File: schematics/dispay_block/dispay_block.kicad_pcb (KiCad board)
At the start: 2 copper layers, 100 x 53.5 mm, 292 parts, among them J1 Conn_02x10_Odd_Even, J2 Conn_02x10_Odd_Even, J3 Conn_02x01, Q1 BC847BS, Q2 BC847BS, Q3 BC847BS, Q4 BC847BS, Q5 BC847BS, Q6 BC847BS, Q7 BC847BS, Q8 BC847BS, U1 CH32V003FxUx

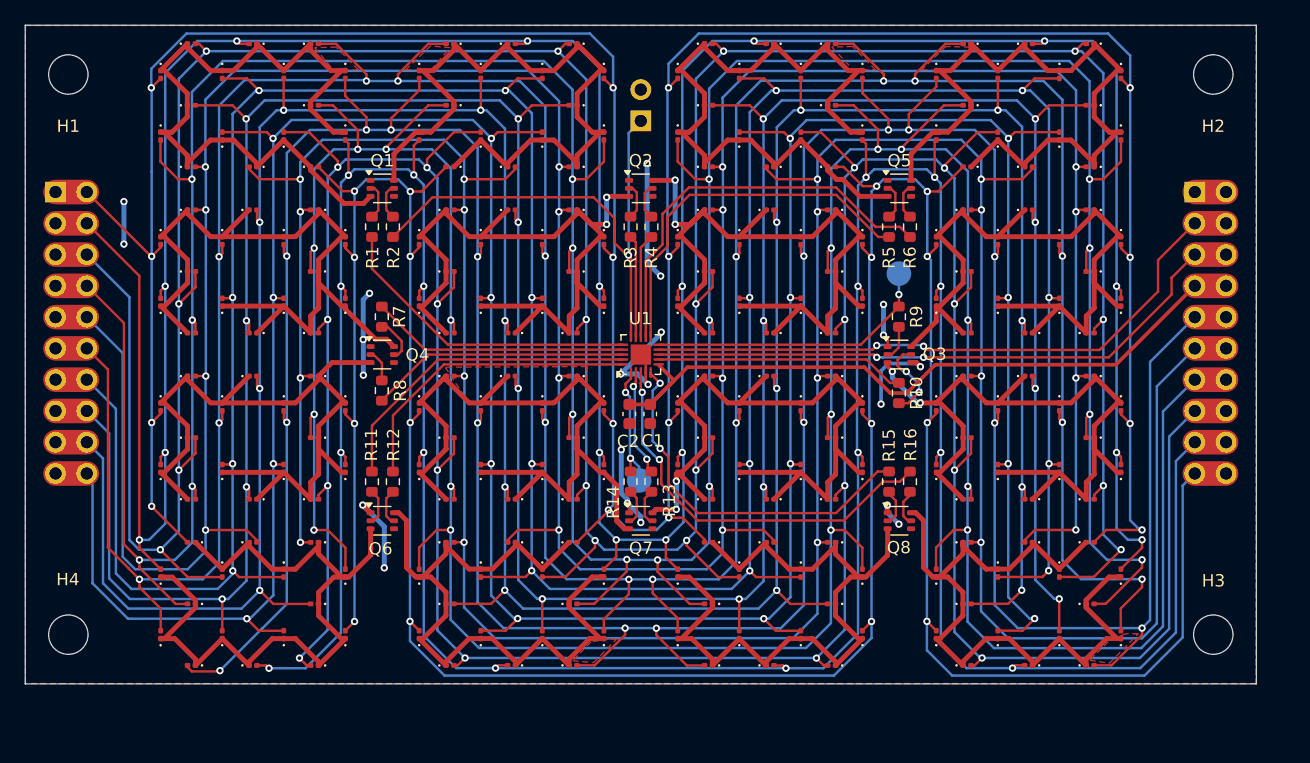
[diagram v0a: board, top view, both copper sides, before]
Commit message: hw: revise display design and fix wrong footprint
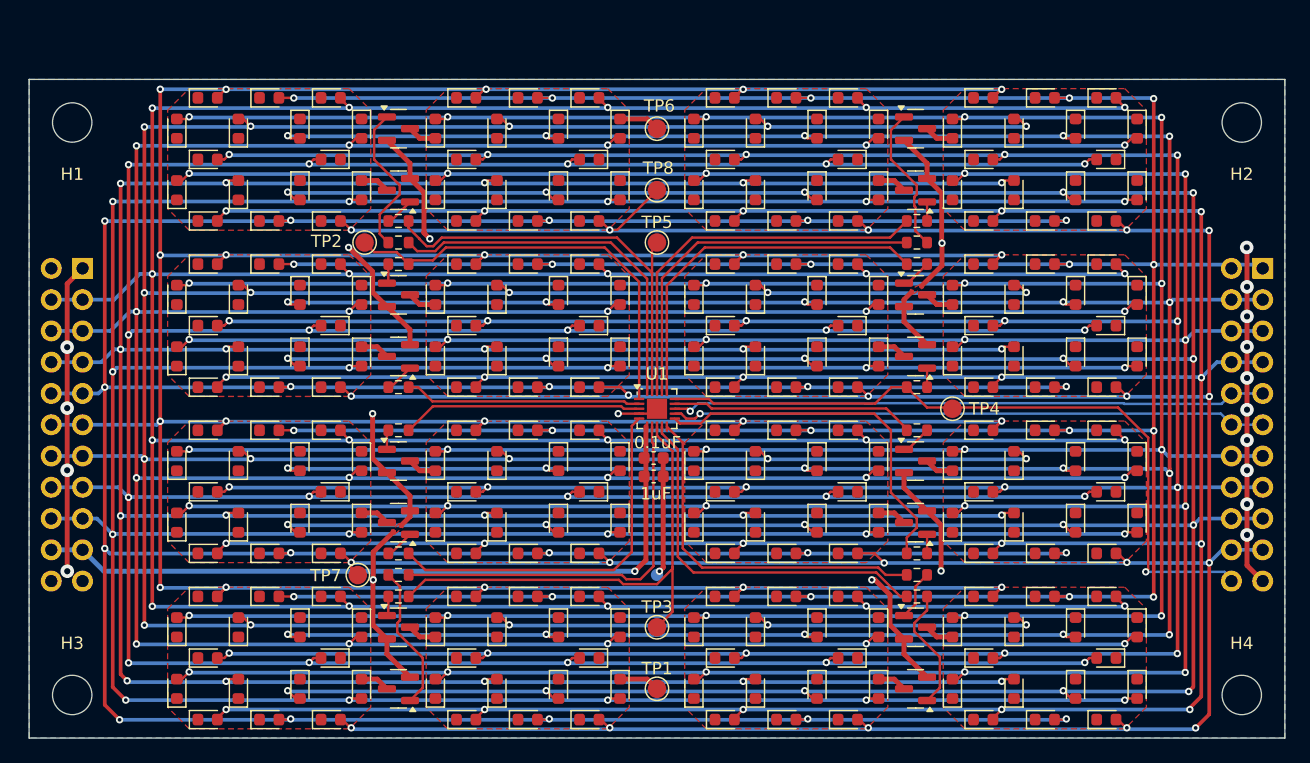
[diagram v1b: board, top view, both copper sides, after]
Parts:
- removed J3: Conn_02x01, Connector_PinHeader_2.54mm:PinHeader_2x01_P2.54mm_Vertical
- added Q10: BC818, Package_TO_SOT_SMD:SOT-23, F.Cu at (172.0, 102.5)
- added Q11: BC818, Package_TO_SOT_SMD:SOT-23, F.Cu at (172.0, 116.0)
- added Q12: BC818, Package_TO_SOT_SMD:SOT-23, F.Cu at (130.0, 124.5)
- added Q13: BC818, Package_TO_SOT_SMD:SOT-23, F.Cu at (130.0, 129.5)
- added Q14: BC818, Package_TO_SOT_SMD:SOT-23, F.Cu at (130.0, 102.5)
- added Q15: BC818, Package_TO_SOT_SMD:SOT-23, F.Cu at (172.0, 129.5)
- added Q16: BC818, Package_TO_SOT_SMD:SOT-23, F.Cu at (130.0, 111.0)
- added Q9: BC818, Package_TO_SOT_SMD:SOT-23, F.Cu at (130.0, 97.5)
- added TP10: GND, TestPoint:TestPoint_Pad_D1.0mm, B.Cu at (151.0, 120.2)
- added TP3: PC1, TestPoint:TestPoint_Pad_D1.5mm, F.Cu at (151.0, 124.5)
- added TP4: PD1(SWIO), TestPoint:TestPoint_Pad_D1.5mm, F.Cu at (175.0, 106.7)
- added TP5: PD5(TX), TestPoint:TestPoint_Pad_D1.5mm, F.Cu at (151.0, 93.2)
- added TP6: CC2, TestPoint:TestPoint_Pad_D1.5mm, F.Cu at (151.0, 84.0)
- added TP7: B8, TestPoint:TestPoint_Pad_D1.5mm, F.Cu at (126.7, 120.3)
- added TP8: B8, TestPoint:TestPoint_Pad_D1.5mm, F.Cu at (151.0, 89.0)
- added TP9: GND, TestPoint:TestPoint_Pad_D1.0mm, B.Cu at (151.0, 93.2)
- D1, D10, D100, D101, D102, D103, D104, D105, D106, D107, D108, D109, D11, D110, D111, D112, D113, D114, D115, D116, D117, D118, D119, D12, D120, D121, D122, D123, D124, D125, D126, D127, D128, D129, D13, D130, D131, D132, D133, D134, D135, D136, D137, D138, D139, D14, D140, D141, D142, D143, D144, D145, D146, D147, D148, D149, D15, D150, D151, D152, D153, D154, D155, D156, D157, D158, D159, D16, D160, D161, D162, D163, D164, D165, D166, D167, D168, D169, D17, D170, D171, D172, D173, D174, D175, D176, D177, D178, D179, D18, D180, D181, D182, D183, D184, D185, D186, D187, D188, D189, D19, D190, D191, D192, D193, D194, D195, D196, D197, D198, D199, D2, D20, D200, D201, D202, D203, D204, D205, D206, D207, D208, D209, D21, D210, D211, D212, D213, D214, D215, D216, D217, D218, D219, D22, D220, D221, D222, D223, D224, D225, D226, D227, D228, D229, D23, D230, D231, D232, D233, D234, D235, D236, D237, D238, D239, D24, D240, D241, D242, D243, D244, D245, D246, D247, D248, D249, D25, D250, D251, D252, D253, D254, D255, D256, D26, D27, D28, D29, D3, D30, D31, D32, D33, D34, D35, D36, D37, D38, D39, D4, D40, D41, D42, D43, D44, D45, D46, D47, D48, D49, D5, D50, D51, D52, D53, D54, D55, D56, D57, D58, D59, D6, D60, D61, D62, D63, D64, D65, D66, D67, D68, D69, D7, D70, D71, D72, D73, D74, D75, D76, D77, D78, D79, D8, D80, D81, D82, D83, D84, D85, D86, D87, D88, D89, D9, D90, D91, D92, D93, D94, D95, D96, D97, D98, D99: footprint LED_SMD:LED_0201_0603Metric -> LED_SMD:LED_0603_1608Metric
- J1, J2: value Conn_02x10_Odd_Even -> Conn_02x11_Odd_Even; footprint Connector_PinSocket_2.54mm:PinSocket_2x10_P2.54mm_Vertical -> Connector_PinHeader_2.54mm:PinHeader_2x11_P2.54mm_Vertical
- Q1, Q2, Q3, Q4, Q5, Q6, Q7, Q8: value BC847BS -> BC818; footprint Package_TO_SOT_SMD:SOT-363_SC-70-6 -> Package_TO_SOT_SMD:SOT-23
- R1, R10, R11, R12, R14, R15, R2, R3, R4, R5, R6, R7, R8, R9: value 270 -> 390
- R13, R16: value 33K -> 390
- TP1: value RESET -> CC13; footprint TestPoint:TestPoint_Pad_D2.0mm -> TestPoint:TestPoint_Pad_D1.5mm; moved to F.Cu
- TP2: value TestPoint -> RESET; footprint TestPoint:TestPoint_Pad_D2.0mm -> TestPoint:TestPoint_Pad_D1.5mm; moved to F.Cu
- moved J1 98.3 mm to (200.2, 95.3)
- moved H4 95.4 mm to (198.5, 130.0), turned to 0 degrees
- moved H3 92.8 mm to (103.5, 130.0), turned to 0 degrees
- moved J2 90.6 mm to (104.3, 95.3)
- moved R2 52.1 mm to (172.1, 122.0), turned to 180 degrees
- moved R6 49.3 mm to (130.0, 118.5), turned to 180 degrees
- moved R1 47.2 mm to (172.1, 108.5), turned to 0 degrees
- moved Q1 44.2 mm to (172.0, 97.5)
- moved R7 43.9 mm to (172.1, 93.2), turned to 0 degrees
- moved TP2 43.5 mm to (127.2, 93.2), turned to 0 degrees
- moved R10 43.3 mm to (130.0, 120.2), turned to 180 degrees
- moved R16 41.8 mm to (130.0, 108.5), turned to 180 degrees
- moved Q5 41.0 mm to (130.0, 84.0)
- moved Q7 38.9 mm to (172.0, 84.0)
- moved D218 35.9 mm to (112.0, 129.5)
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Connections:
- C1 pad 2: +3V3 -> +5V
- C2 pad 2: +3V3 -> +5V
- D1 pad 2: A_1 -> A_13
- D10 pad 2: B_2 -> A_3
- D100 pad 2: B_6 -> A_5
- D101 pad 2: B_2 -> A_14
- D102 pad 2: A_7 -> A_2
- D103 pad 2: B_5 -> A_10
- D105 pad 2: B_8 -> A_15
- D106 pad 2: A_2 -> A_3
- D107 pad 2: A_8 -> A_11
- D108 pad 2: B_1 -> A_7
- D109 pad 2: B_3 -> A_16
- D11 pad 2: B_3 -> A_11
- D110 pad 2: B_4 -> A_4
- D111 pad 2: A_3 -> A_12
- D112 pad 2: B_7 -> A_8
- D113 pad 2: A_5 -> A_13
- D115 pad 2: A_4 -> A_9
- D116 pad 2: B_6 -> A_5
- D117 pad 2: B_2 -> A_14
- D118 pad 2: A_7 -> A_2
- D119 pad 2: B_5 -> A_10
- D12 pad 2: B_4 -> A_7
- D121 pad 2: B_8 -> A_15
- D122 pad 2: A_2 -> A_3
- D123 pad 2: A_8 -> A_11
- D124 pad 2: B_1 -> A_7
- D125 pad 2: B_3 -> A_16
- D126 pad 2: B_4 -> A_4
- D127 pad 2: A_3 -> A_12
- D128 pad 2: B_7 -> A_8
- D129 pad 2: A_5 -> A_13
- D13 pad 2: B_5 -> A_16
- D131 pad 2: A_4 -> A_9
- D132 pad 2: B_6 -> A_5
- D133 pad 2: B_2 -> A_14
- D134 pad 2: A_7 -> A_2
- D135 pad 2: B_5 -> A_10
- D137 pad 2: B_8 -> A_15
- D138 pad 2: A_2 -> A_3
- D139 pad 2: A_8 -> A_11
- D14 pad 2: B_6 -> A_4
- D140 pad 2: B_1 -> A_7
- D141 pad 2: B_3 -> A_16
- D142 pad 2: B_4 -> A_4
- D143 pad 2: A_3 -> A_12
- D144 pad 2: B_7 -> A_8
- D145 pad 2: A_5 -> A_13
- D147 pad 2: A_4 -> A_9
- D148 pad 2: B_6 -> A_5
- D149 pad 2: B_2 -> A_14
- D15 pad 2: B_7 -> A_12
- D150 pad 2: A_7 -> A_2
- D151 pad 2: B_5 -> A_10
- D153 pad 2: B_8 -> A_15
- D154 pad 2: A_2 -> A_3
- D155 pad 2: A_8 -> A_11
- D156 pad 2: B_1 -> A_7
- D157 pad 2: B_3 -> A_16
- D158 pad 2: B_4 -> A_4
- D159 pad 2: A_3 -> A_12
- D16 pad 2: B_8 -> A_8
- D160 pad 2: B_7 -> A_8
- D161 pad 2: A_5 -> A_13
- D163 pad 2: A_4 -> A_9
- D164 pad 2: B_6 -> A_5
- D165 pad 2: B_2 -> A_14
- D166 pad 2: A_7 -> A_2
- D167 pad 2: B_5 -> A_10
- D169 pad 2: B_8 -> A_15
- D17 pad 2: A_5 -> A_13
- D170 pad 2: A_2 -> A_3
- D171 pad 2: A_8 -> A_11
- D172 pad 2: B_1 -> A_7
- D173 pad 2: B_3 -> A_16
- D174 pad 2: B_4 -> A_4
- D175 pad 2: A_3 -> A_12
- D176 pad 2: B_7 -> A_8
- D177 pad 2: A_5 -> A_13
- D179 pad 2: A_4 -> A_9
- D180 pad 2: B_6 -> A_5
- D181 pad 2: B_2 -> A_14
- D182 pad 2: A_7 -> A_2
- D183 pad 2: B_5 -> A_10
- D185 pad 2: B_8 -> A_15
- D186 pad 2: A_2 -> A_3
- D187 pad 2: A_8 -> A_11
- D188 pad 2: B_1 -> A_7
- D189 pad 2: B_3 -> A_16
- D19 pad 2: A_4 -> A_9
- D190 pad 2: B_4 -> A_4
- D191 pad 2: A_3 -> A_12
- D192 pad 2: B_7 -> A_8
- D193 pad 2: A_5 -> A_13
- D195 pad 2: A_4 -> A_9
- D196 pad 2: B_6 -> A_5
- D197 pad 2: B_2 -> A_14
- D198 pad 2: A_7 -> A_2
- D199 pad 2: B_5 -> A_10
- D2 pad 2: A_2 -> A_1
- D20 pad 2: B_6 -> A_5
- D201 pad 2: B_8 -> A_15
- D202 pad 2: A_2 -> A_3
- D203 pad 2: A_8 -> A_11
- D204 pad 2: B_1 -> A_7
- D205 pad 2: B_3 -> A_16
- D206 pad 2: B_4 -> A_4
- D207 pad 2: A_3 -> A_12
- D208 pad 2: B_7 -> A_8
- D209 pad 2: A_5 -> A_13
- D21 pad 2: B_2 -> A_14
- D211 pad 2: A_4 -> A_9
- D212 pad 2: B_6 -> A_5
- D213 pad 2: B_2 -> A_14
- D214 pad 2: A_7 -> A_2
- D215 pad 2: B_5 -> A_10
- D217 pad 2: B_8 -> A_15
- D218 pad 2: A_2 -> A_3
- D219 pad 2: A_8 -> A_11
- D22 pad 2: A_7 -> A_2
- D220 pad 2: B_1 -> A_7
- D221 pad 2: B_3 -> A_16
- D222 pad 2: B_4 -> A_4
- D223 pad 2: A_3 -> A_12
- D224 pad 2: B_7 -> A_8
- D225 pad 2: A_5 -> A_13
- D227 pad 2: A_4 -> A_9
- D228 pad 2: B_6 -> A_5
- D229 pad 2: B_2 -> A_14
- D23 pad 2: B_5 -> A_10
- D230 pad 2: A_7 -> A_2
- D231 pad 2: B_5 -> A_10
- D233 pad 2: B_8 -> A_15
- D234 pad 2: A_2 -> A_3
- D235 pad 2: A_8 -> A_11
- D236 pad 2: B_1 -> A_7
- D237 pad 2: B_3 -> A_16
- D238 pad 2: B_4 -> A_4
- D239 pad 2: A_3 -> A_12
- D240 pad 2: B_7 -> A_8
- D241 pad 2: A_5 -> A_13
- D243 pad 2: A_4 -> A_9
- D244 pad 2: B_6 -> A_5
- D245 pad 2: B_2 -> A_14
- D246 pad 2: A_7 -> A_2
- D247 pad 2: B_5 -> A_10
- D249 pad 2: B_8 -> A_15
- D25 pad 2: B_8 -> A_15
- D250 pad 2: A_2 -> A_3
- D251 pad 2: A_8 -> A_11
- D252 pad 2: B_1 -> A_7
- D253 pad 2: B_3 -> A_16
- D254 pad 2: B_4 -> A_4
- D255 pad 2: A_3 -> A_12
- D256 pad 2: B_7 -> A_8
- D26 pad 2: A_2 -> A_3
- D27 pad 2: A_8 -> A_11
- D28 pad 2: B_1 -> A_7
- D29 pad 2: B_3 -> A_16
- D3 pad 2: A_3 -> A_9
- D30 pad 2: B_4 -> A_4
- D31 pad 2: A_3 -> A_12
- D32 pad 2: B_7 -> A_8
- D33 pad 2: A_5 -> A_13
- D35 pad 2: A_4 -> A_9
- D36 pad 2: B_6 -> A_5
- D37 pad 2: B_2 -> A_14
- D38 pad 2: A_7 -> A_2
- D39 pad 2: B_5 -> A_10
- D4 pad 2: A_4 -> A_5
- D41 pad 2: B_8 -> A_15
- D42 pad 2: A_2 -> A_3
- D43 pad 2: A_8 -> A_11
- D44 pad 2: B_1 -> A_7
- D45 pad 2: B_3 -> A_16
- D46 pad 2: B_4 -> A_4
- D47 pad 2: A_3 -> A_12
- D48 pad 2: B_7 -> A_8
- D49 pad 2: A_5 -> A_13
- D5 pad 2: A_5 -> A_14
- D51 pad 2: A_4 -> A_9
- D52 pad 2: B_6 -> A_5
- D53 pad 2: B_2 -> A_14
- D54 pad 2: A_7 -> A_2
- D55 pad 2: B_5 -> A_10
- D57 pad 2: B_8 -> A_15
- D58 pad 2: A_2 -> A_3
- D59 pad 2: A_8 -> A_11
- D6 pad 2: A_6 -> A_2
- D60 pad 2: B_1 -> A_7
- D61 pad 2: B_3 -> A_16
- D62 pad 2: B_4 -> A_4
- D63 pad 2: A_3 -> A_12
- D64 pad 2: B_7 -> A_8
- D65 pad 2: A_5 -> A_13
- D67 pad 2: A_4 -> A_9
- D68 pad 2: B_6 -> A_5
- D69 pad 2: B_2 -> A_14
- D7 pad 2: A_7 -> A_10
- D70 pad 2: A_7 -> A_2
- D71 pad 2: B_5 -> A_10
- D73 pad 2: B_8 -> A_15
- D74 pad 2: A_2 -> A_3
- D75 pad 2: A_8 -> A_11
- D76 pad 2: B_1 -> A_7
- D77 pad 2: B_3 -> A_16
- D78 pad 2: B_4 -> A_4
- D79 pad 2: A_3 -> A_12
- D8 pad 2: A_8 -> A_6
- D80 pad 2: B_7 -> A_8
- D81 pad 2: A_5 -> A_13
- D83 pad 2: A_4 -> A_9
- D84 pad 2: B_6 -> A_5
- D85 pad 2: B_2 -> A_14
- D86 pad 2: A_7 -> A_2
- D87 pad 2: B_5 -> A_10
- D89 pad 2: B_8 -> A_15
- D9 pad 2: B_1 -> A_15
- D90 pad 2: A_2 -> A_3
- D91 pad 2: A_8 -> A_11
- D92 pad 2: B_1 -> A_7
- D93 pad 2: B_3 -> A_16
- D94 pad 2: B_4 -> A_4
- D95 pad 2: A_3 -> A_12
- D96 pad 2: B_7 -> A_8
- D97 pad 2: A_5 -> A_13
- D99 pad 2: A_4 -> A_9
- J1 pad 10: A_5 -> /SDA
- J1 pad 11: A_6 -> /SCL
- J1 pad 12: A_6 -> /SCL
- J1 pad 13: A_7 -> A_5
- J1 pad 14: A_7 -> A_5
- J1 pad 15: A_8 -> A_6
- J1 pad 16: A_8 -> A_6
- J1 pad 17: B_1 -> A_7
- J1 pad 18: B_1 -> A_7
- J1 pad 19: B_2 -> A_8
- J1 pad 20: B_2 -> A_8
- J1 pad 9: A_5 -> /SDA
- J2 pad 10: B_3 -> A_12
- J2 pad 11: B_4 -> A_13
- J2 pad 12: B_4 -> A_13
- J2 pad 13: B_5 -> A_14
- J2 pad 14: B_5 -> A_14
- J2 pad 15: B_6 -> A_15
- J2 pad 16: B_6 -> A_15
- J2 pad 17: B_7 -> A_16
- J2 pad 18: B_7 -> A_16
- J2 pad 19: B_8 -> +5V
- J2 pad 20: B_8 -> +5V
- J2 pad 3: /SCL -> A_9
- J2 pad 4: /SCL -> A_9
- J2 pad 5: /SDA -> A_10
- J2 pad 6: /SDA -> A_10
- J2 pad 7: +3V3 -> A_11
- J2 pad 8: +3V3 -> A_11
- J2 pad 9: B_3 -> A_12
- Q1 pad 1: GND -> Net-(Q1-B)
- Q1 pad 2: Net-(Q1A-B1) -> GND
- Q1 pad 3: /CC1 -> /CC8
- Q2 pad 1: GND -> Net-(Q2-B)
- Q2 pad 2: Net-(Q2A-B1) -> GND
- Q2 pad 3: /CC6 -> /CC12
- Q3 pad 1: GND -> Net-(Q3-B)
- Q3 pad 2: Net-(Q3A-B1) -> GND
- Q3 pad 3: /CC12 -> /CC16
- Q4 pad 1: GND -> Net-(Q4-B)
- Q4 pad 2: Net-(Q4A-B1) -> GND
- Q4 pad 3: /CC9 -> /CC1
- Q5 pad 1: GND -> Net-(Q5-B)
- Q5 pad 2: Net-(Q5A-B1) -> GND
- Q5 pad 3: /CC3 -> /CC2
- Q6 pad 1: GND -> Net-(Q6-B)
- Q6 pad 2: Net-(Q6A-B1) -> GND
- Q6 pad 3: /CC13 -> /CC9
- Q7 pad 1: GND -> Net-(Q7-B)
- Q7 pad 2: Net-(Q7A-B1) -> GND
- Q7 pad 3: /CC10 -> /CC4
- Q8 pad 1: GND -> Net-(Q8-B)
- Q8 pad 2: Net-(Q8A-B1) -> GND
- Q8 pad 3: /CC15 -> /CC3
- R1 pad 1: Net-(U1-PD2) -> Net-(U1-PC7)
- R1 pad 2: Net-(Q1A-B1) -> Net-(Q2-B)
- R10 pad 2: Net-(Q3B-B2) -> Net-(Q13-B)
- R11 pad 1: Net-(U1-PD5) -> Net-(Q9-B)
- R11 pad 2: Net-(Q6A-B1) -> Net-(U1-PD7)
- R12 pad 1: Net-(U1-PD6) -> Net-(Q12-B)
- R12 pad 2: Net-(Q6B-B2) -> Net-(U1-PC1)
- R13 pad 1: Net-(U1-PA1) -> /SWIO
- R13 pad 2: Net-(Q7B-B2) -> Net-(Q10-B)
- R14 pad 1: Net-(U1-PD7) -> Net-(U1-PC4)
- R14 pad 2: Net-(Q7A-B1) -> Net-(Q11-B)
- R15 pad 1: Net-(U1-PD0) -> Net-(Q3-B)
- R15 pad 2: Net-(Q8A-B1) -> Net-(U1-PC3)
- R16 pad 2: Net-(Q8B-B2) -> Net-(Q16-B)
- R2 pad 1: /SWIO -> Net-(Q15-B)
- R2 pad 2: Net-(Q1B-B2) -> Net-(U1-PC2)
- R3 pad 1: Net-(U1-PC7) -> Net-(Q4-B)
- R3 pad 2: Net-(Q2A-B1) -> Net-(U1-PD5)
- R4 pad 1: Net-(U1-PC6) -> Net-(Q5-B)
- R4 pad 2: Net-(Q2B-B2) -> Net-(U1-PD6)
- R5 pad 1: Net-(U1-PC4) -> Net-(U1-PD2)
- R5 pad 2: Net-(Q5A-B1) -> Net-(Q1-B)
- R6 pad 1: Net-(U1-PC5) -> Net-(U1-PD0)
- R6 pad 2: Net-(Q5B-B2) -> Net-(Q6-B)
- R7 pad 2: Net-(Q4B-B2) -> Net-(Q7-B)
- R8 pad 1: Net-(U1-PD4) -> Net-(U1-PA1)
- R8 pad 2: Net-(Q4A-B1) -> Net-(Q14-B)
- R9 pad 1: Net-(U1-PC3) -> Net-(Q8-B)
- R9 pad 2: Net-(Q3A-B1) -> Net-(U1-PD4)
- TP1 pad 1: Net-(U1-PD7) -> /CC13
- TP2 pad 1: Net-(U1-PC3) -> Net-(U1-PD7)
- U1 pad 12: Net-(U1-PC5) -> /SCL
- U1 pad 13: Net-(U1-PC6) -> /SDA
- U1 pad 6: +3V3 -> +5V
- U1 pad 8: /SDA -> Net-(U1-PC1)
- U1 pad 9: /SCL -> Net-(U1-PC2)
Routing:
- net A_16: track 0.00 -> 391.2 mm, vias 0 -> 20
- net A_10: track 0.00 -> 388.9 mm, vias 0 -> 20
- net A_9: track 0.00 -> 382.2 mm, vias 0 -> 20
- net A_15: track 0.00 -> 375.7 mm, vias 0 -> 20
- net A_12: track 0.00 -> 372.8 mm, vias 0 -> 20
- net A_14: track 0.00 -> 353.9 mm, vias 0 -> 20
- net A_13: track 0.00 -> 353.8 mm, vias 0 -> 20
- net A_11: track 0.00 -> 349.7 mm, vias 0 -> 20
- net B_3: track 307.6 -> 0.00 mm, vias 16 -> 0
- net B_5: track 295.0 -> 0.00 mm, vias 16 -> 0
- net B_6: track 292.2 -> 0.00 mm, vias 16 -> 0
- net B_1: track 282.0 -> 0.00 mm, vias 16 -> 0
- net B_2: track 281.9 -> 0.00 mm, vias 16 -> 0
- net B_7: track 272.2 -> 0.00 mm, vias 16 -> 0
- net B_4: track 271.8 -> 0.00 mm, vias 16 -> 0
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- added copper zone on F.Cu, net /CC1
- added copper zone on F.Cu, net /CC10
- added copper zone on F.Cu, net /CC11
- added copper zone on F.Cu, net /CC12
- added copper zone on F.Cu, net /CC13
- added copper zone on F.Cu, net /CC14
- added copper zone on F.Cu, net /CC15
- added copper zone on F.Cu, net /CC16
- added copper zone on F.Cu, net /CC2
- added copper zone on F.Cu, net /CC3
- added copper zone on F.Cu, net /CC4
- added copper zone on F.Cu, net /CC5
- added copper zone on F.Cu, net /CC6
- added copper zone on F.Cu, net /CC7
- added copper zone on F.Cu, net /CC8
- added copper zone on F.Cu, net /CC9
- added copper zone on B.Cu, net GND
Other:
- board size 100 x 53.5 mm -> 102 x 53.5 mm
- board text added: "+5V"
- board text added: "ALL RESISTORS 390Ω"
- board text added: "ALL TRANSISTORS BC818"
- board text added: "A_1"
- board text added: "A_10"
- board text added: "A_11"
- board text added: "A_12"
- board text added: "A_13"
- board text added: "A_14"
- board text added: "A_15"
- board text added: "A_16"
- board text added: "A_2"
- board text added: "A_3"
- board text added: "A_4"
- board text added: "A_5"
- board text added: "A_6"
- board text added: "A_7"
- board text added: "A_8"
- board text added: "A_9"
- board text removed: "3.3V"
- board text removed: "A1"
- board text removed: "A2"
- board text removed: "A3"
- board text removed: "A4"
- board text removed: "A5"
- board text removed: "A6"
- board text removed: "A7"
- board text removed: "A8"
- board text removed: "ALL RESISTORS 270Ω"
- board text removed: "B1"
- board text removed: "B2"
- board text removed: "B3"
- board text removed: "B4"
- board text removed: "B5"
- board text removed: "B6"
- board text removed: "B7"
- board text removed: "B8"
